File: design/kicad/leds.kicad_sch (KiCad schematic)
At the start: 0 parts

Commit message: completes kicad schematic, starts pcb layout
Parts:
- added C10, C11, C14: 0.1uF, Capacitor_SMD:C_0402_1005Metric, symbol Device:C
- added LED_1, LED_10, LED_11, LED_12, LED_13, LED_14, LED_15, LED_16, LED_17, LED_18, LED_19, LED_2, LED_20, LED_21, LED_22, LED_23, LED_24, LED_25, LED_26, LED_27, LED_28, LED_29, LED_3, LED_30, LED_31, LED_32, LED_33, LED_34, LED_35, LED_36, LED_37, LED_38, LED_39, LED_4, LED_40, LED_41, LED_42, LED_43, LED_44, LED_45, LED_46, LED_47, LED_48, LED_5, LED_6, LED_7, LED_8, LED_9: White, LED_SMD:LED_PLCC-2_3.4x3.0mm_AK, symbol Device:LED
- added R10, R24, R37, R38, R88, R89: 4.7K, Resistor_SMD:R_0603_1608Metric, symbol Device:R
- added R23, R25, R26, R27, R28, R29, R30, R31, R32, R33, R34, R35, R36, R39, R40, R41, R42, R43, R44, R45, R46, R47, R48, R49, R50, R51, R52, R53, R54, R7, R72, R73, R74, R75, R76, R77, R78, R79, R8, R80, R81, R82, R83, R84, R85, R86, R87, R9: 140R, Resistor_SMD:R_0603_1608Metric, symbol Device:R
- added U3, U7, U8: PCA9685PW, Package_SO:TSSOP-28_4.4x9.7mm_P0.65mm, symbol Driver_LED:PCA9685PW
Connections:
- new net: LED_19.1 (K), R41.2
- new net: LED_29.1 (K), R51.2
- new net: LED_36.1 (K), R75.2
- new net: LED_40.1 (K), R79.2
- new net: LED_27.1 (K), R49.2
- new net: LED_23.1 (K), R45.2
- new net: LED_38.1 (K), R77.2
- new net: LED_35.1 (K), R74.2
- new net: LED_14.1 (K), R34.2
- new net: LED_24.1 (K), R46.2
- new net: LED_20.1 (K), R42.2
- new net: LED_39.1 (K), R78.2
- new net: LED_18.1 (K), R40.2
- new net: LED_16.1 (K), R36.2
- new net: LED_45.1 (K), R84.2
- new net: LED_42.1 (K), R81.2
- new net: LED_1.1 (K), R7.2
- new net: LED_25.1 (K), R47.2
- new net: LED_2.1 (K), R8.2
- new net: LED_6.1 (K), R26.2
- new net: LED_17.1 (K), R39.2
- new net: LED_8.1 (K), R28.2
- new net: LED_28.1 (K), R50.2
- new net: LED_34.1 (K), R73.2
- new net: LED_11.1 (K), R31.2
- new net: LED_48.1 (K), R87.2
- new net: LED_26.1 (K), R48.2
- new net: LED_47.1 (K), R86.2
- new net: LED_4.1 (K), R23.2
- new net: LED_5.1 (K), R25.2
- new net: LED_41.1 (K), R80.2
- new net: LED_13.1 (K), R33.2
- new net: LED_31.1 (K), R53.2
- new net: LED_9.1 (K), R29.2
- new net: LED_22.1 (K), R44.2
- new net: LED_32.1 (K), R54.2
- new net: LED_21.1 (K), R43.2
- new net: LED_37.1 (K), R76.2
- new net: LED_43.1 (K), R82.2
- new net: LED_10.1 (K), R30.2
- new net: LED_12.1 (K), R32.2
- new net: LED_30.1 (K), R52.2
- new net: LED_46.1 (K), R85.2
- new net: LED_44.1 (K), R83.2
- new net: LED_3.1 (K), R9.2
- new net: LED_15.1 (K), R35.2
- new net: LED_33.1 (K), R72.2
- new net: LED_7.1 (K), R27.2
- new net 5V: C10.1, C11.1, C14.1, LED_1.2 (A), LED_10.2 (A), LED_11.2 (A), LED_12.2 (A), LED_13.2 (A), LED_14.2 (A), LED_15.2 (A), LED_16.2 (A), LED_17.2 (A), LED_18.2 (A), LED_19.2 (A), LED_2.2 (A), LED_20.2 (A), LED_21.2 (A), LED_22.2 (A), LED_23.2 (A), LED_24.2 (A), LED_25.2 (A), LED_26.2 (A), LED_27.2 (A), LED_28.2 (A), LED_29.2 (A), LED_3.2 (A), LED_30.2 (A), LED_31.2 (A), LED_32.2 (A), LED_33.2 (A), LED_34.2 (A), LED_35.2 (A), LED_36.2 (A), LED_37.2 (A), LED_38.2 (A), LED_39.2 (A), LED_4.2 (A), LED_40.2 (A), LED_41.2 (A), LED_42.2 (A), LED_43.2 (A), LED_44.2 (A), LED_45.2 (A), LED_46.2 (A), LED_47.2 (A), LED_48.2 (A), LED_5.2 (A), LED_6.2 (A), LED_7.2 (A), LED_8.2 (A), LED_9.2 (A), R10.2, R24.2, R37.2, R38.2, R88.2, R89.2, U3.2 (A1), U3.28 (VDD), U7.2 (A1), U7.28 (VDD), U8.2 (A1), U8.28 (VDD)
- new net GND: C10.2, C11.2, C14.2, U3.1 (A0), U3.14 (VSS), U3.23 (~{OE}), U3.24 (A5), U3.25 (EXTCLK), U3.3 (A2), U3.4 (A3), U3.5 (A4), U7.1 (A0), U7.14 (VSS), U7.23 (~{OE}), U7.24 (A5), U7.25 (EXTCLK), U7.3 (A2), U7.4 (A3), U7.5 (A4), U8.1 (A0), U8.14 (VSS), U8.23 (~{OE}), U8.24 (A5), U8.25 (EXTCLK), U8.3 (A2), U8.4 (A3), U8.5 (A4)
- new net LED_1: R7.1, U8.11 (LED5)
- new net LED_10: R30.1, U8.6 (LED0)
- new net LED_11: R31.1, U7.12 (LED6)
- new net LED_12: R32.1, U7.13 (LED7)
- new net LED_13: R33.1, U7.11 (LED5)
- new net LED_14: R34.1, U3.12 (LED6), U7.15 (LED8)
- new net LED_15: R35.1, U3.13 (LED7)
- new net LED_16: R36.1, U3.16 (LED9)
- new net LED_17: R39.1, U3.15 (LED8)
- new net LED_18: R40.1, U3.17 (LED10)
- new net LED_19: R41.1, U3.18 (LED11)
- new net LED_2: R8.1, U8.9 (LED3)
- new net LED_20: R42.1, U8.17 (LED10)
- new net LED_21: R43.1, U8.12 (LED6)
- new net LED_22: R44.1, U8.8 (LED2)
- new net LED_23: R45.1, U7.7 (LED1)
- new net LED_24: R46.1, U7.20 (LED13)
- new net LED_25: R47.1, U7.18 (LED11)
- new net LED_26: R48.1, U3.6 (LED0), U7.16 (LED9)
- new net LED_27: R49.1, U3.8 (LED2)
- new net LED_28: R50.1, U3.10 (LED4)
- new net LED_29: R51.1, U3.19 (LED12)
- new net LED_3: R9.1, U7.8 (LED2)
- new net LED_30: R52.1, U8.10 (LED4)
- new net LED_31: R53.1
- new net LED_32: R54.1, U8.15 (LED8)
- new net LED_33: R72.1, U8.16 (LED9)
- new net LED_34: R73.1, U3.9 (LED3)
- new net LED_35: R74.1, U3.22 (LED15)
- new net LED_36: R75.1, U3.21 (LED14)
- new net LED_37: R76.1, U3.20 (LED13)
- new net LED_38: R77.1, U8.13 (LED7)
- new net LED_39: R78.1, U7.10 (LED4), U7.9 (LED3), U8.7 (LED1)
- new net LED_4: R23.1
- new net LED_40: R79.1, U7.6 (LED0)
- new net LED_41: R80.1, U7.21 (LED14)
- new net LED_42: R81.1, U7.22 (LED15)
- new net LED_43: R82.1
- new net LED_44: R83.1
- new net LED_45: R84.1, U8.19 (LED12)
- new net LED_46: R85.1, U8.20 (LED13)
- new net LED_47: R86.1, U8.21 (LED14)
- new net LED_48: R87.1, U8.22 (LED15)
- new net LED_5: R25.1, U7.19 (LED12)
- new net LED_6: R26.1, U7.17 (LED10)
- new net LED_7: R27.1, U3.7 (LED1)
- new net LED_8: R28.1, U3.11 (LED5)
- new net LED_9: R29.1, U8.18 (LED11)
- new net SCL: R10.1, R37.1, R88.1, U3.26 (SCL), U7.26 (SCL), U8.26 (SCL)
- new net SDA: R24.1, R38.1, R89.1, U3.27 (SDA), U7.27 (SDA), U8.27 (SDA)
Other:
- note added: "Only buttons that can be latched need LEDS, this includes all mod buttons and discludes Empty and Settings. But since there are 16 leds for buttons plus 16 more for modes and side buttons, conservation of leds can be thrown out as a 3rd chip is then required. So no conservation of leds necessary"

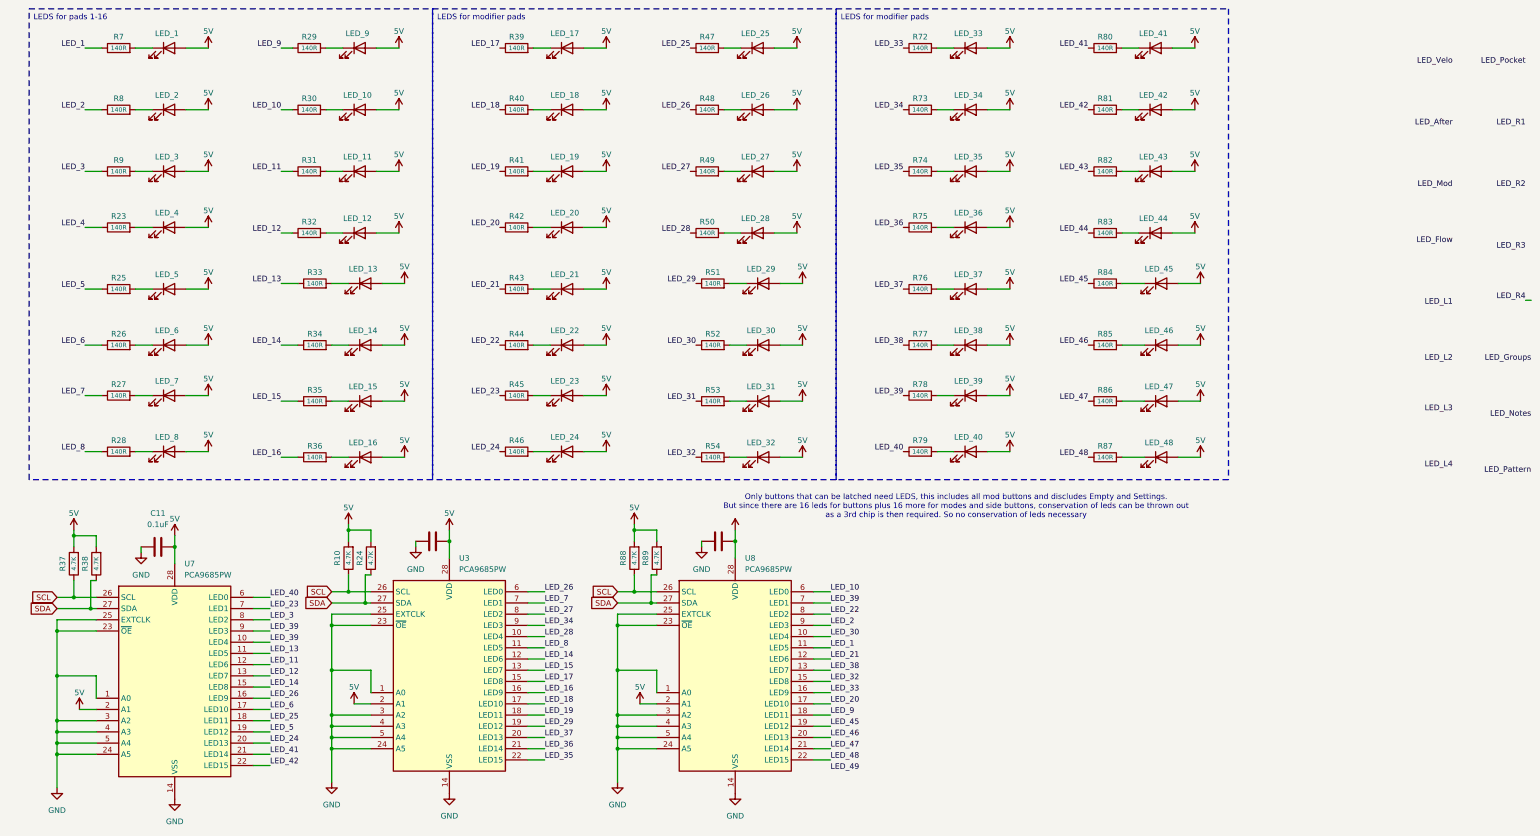
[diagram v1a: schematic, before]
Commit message: routes PCB all except PWR
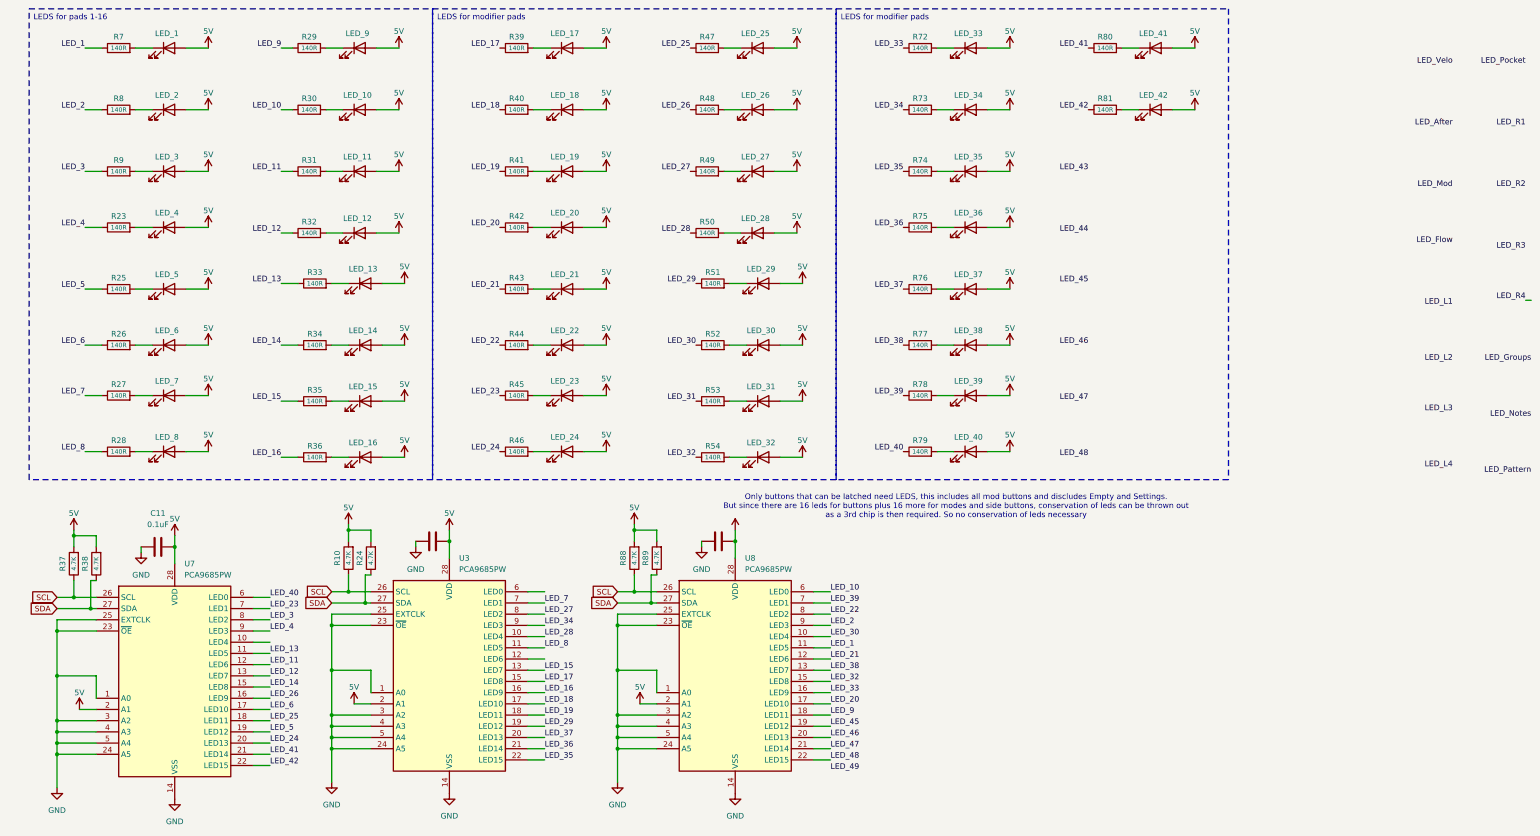
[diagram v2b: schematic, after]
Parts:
- removed LED_43, LED_44, LED_45, LED_46, LED_47, LED_48: White, LED_SMD:LED_PLCC-2_3.4x3.0mm_AK, symbol Device:LED
- removed R82, R83, R84, R85, R86, R87: 140R, Resistor_SMD:R_0603_1608Metric, symbol Device:R
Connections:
- net LED_14: no longer U3.12 (LED6)
- net LED_26: no longer U3.6 (LED0)
- net LED_39: no longer U7.10 (LED4), U7.9 (LED3)
- net LED_4: now also U7.9 (LED3)

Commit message: shortens SD data lines
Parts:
- R23, R25, R26, R27, R28, R29, R30, R31, R32, R33, R34, R35, R36, R39, R40, R41, R42, R43, R44, R45, R46, R47, R48, R49, R50, R51, R52, R53, R54, R7, R72, R73, R74, R75, R76, R77, R78, R79, R8, R80, R81, R9: value 140R -> 150R; LCSC (none) -> C22808
- U3, U7, U8: LCSC C2688894 -> C2678753
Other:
- note added: "was 140R for all LED resistors but not in stock"

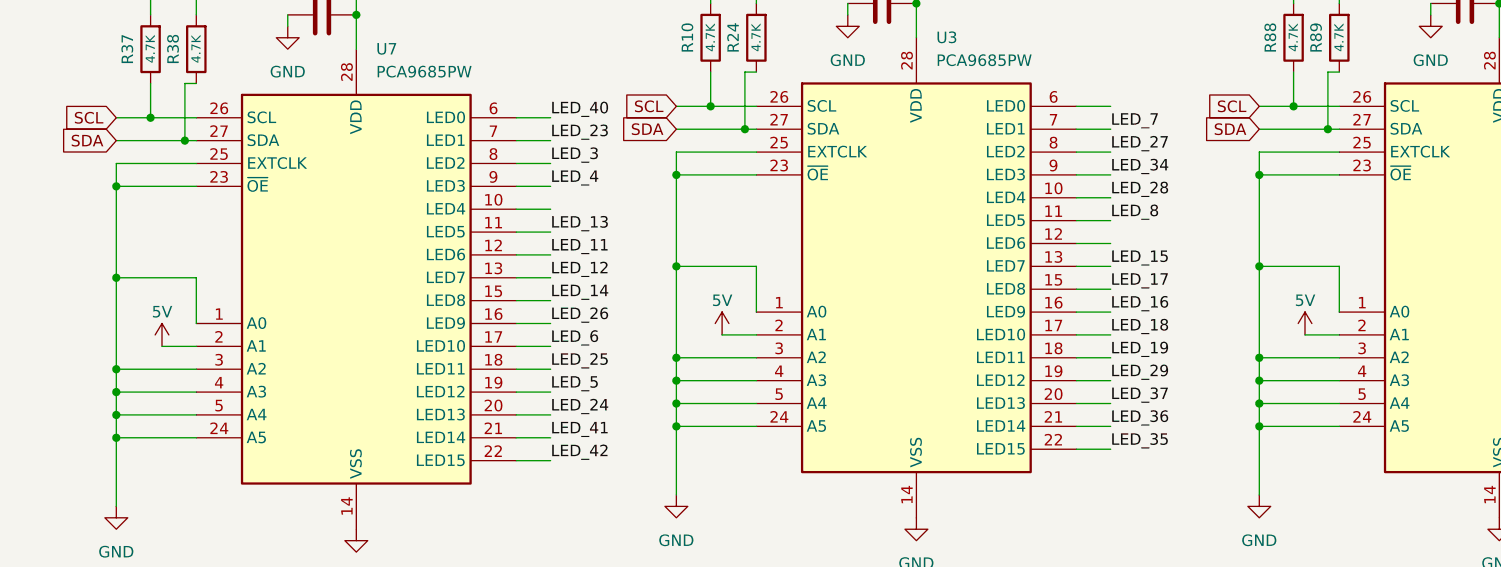
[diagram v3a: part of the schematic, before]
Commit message: pcb rules fixes, reroute suggestions
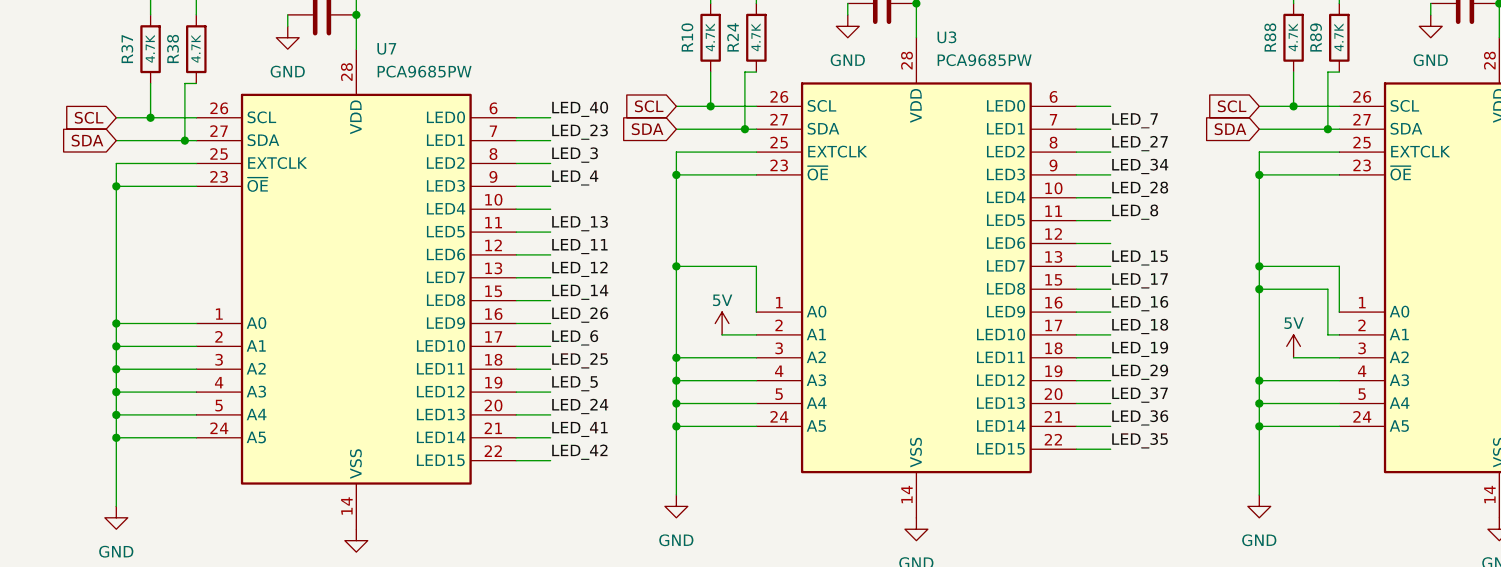
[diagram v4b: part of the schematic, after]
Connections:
- net 5V: now also C14.2, U8.3 (A2); no longer C14.1, U7.2 (A1), U8.2 (A1)
- net GND: now also C14.1, U7.2 (A1), U8.2 (A1); no longer C14.2, U8.3 (A2)
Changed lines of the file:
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@@
 	(paper "A4")
 	(junction
+		(at 146.05 165.1)
+		(diameter 0)
+		(color 0 0 0 0)
+	)
+	(junction
 		(at 146.05 177.8)
 		(diameter 0)
@@
 	)
 	(junction
+		(at 19.05 171.45)
+		(diameter 0)
+		(color 0 0 0 0)
+	)
+	(junction
 		(at 22.86 146.05)
 		(diameter 0)
@@
 	)
 	(junction
-		(at 146.05 175.26)
+		(at 19.05 168.91)
 		(diameter 0)
 		(color 0 0 0 0)
 	)
 	(junction
-		(at 146.05 180.34)
+		(at 146.05 175.26)
 		(diameter 0)
 		(color 0 0 0 0)
 	)
 	(junction
-		(at 19.05 176.53)
+		(at 146.05 180.34)
 		(diameter 0)
 		(color 0 0 0 0)
 	)
 	(junction
-		(at 149.86 130.81)
+		(at 19.05 176.53)
 		(diameter 0)
 		(color 0 0 0 0)
 	)
 	(junction
-		(at 19.05 163.83)
+		(at 149.86 130.81)
 		(diameter 0)
 		(color 0 0 0 0)
@@
 	)
 	(junction
-		(at 146.05 172.72)
-		(diameter 0)
-		(color 0 0 0 0)
-	)
-	(junction
 		(at 85.09 144.78)
 		(diameter 0)
@@
 	(wire
 		(pts
-			(xy 27.94 168.91) (xy 27.94 163.83)
-		)
-		(stroke
-			(width 0)
-			(type default)
-		)
-	)
-	(wire
-		(pts
 			(xy 97.79 74.93) (xy 92.71 74.93)
 		)
@@
 	(wire
 		(pts
+			(xy 154.94 170.18) (xy 153.67 170.18)
+		)
+		(stroke
+			(width 0)
+			(type default)
+		)
+	)
+	(wire
+		(pts
 			(xy 143.51 100.33) (xy 138.43 100.33)
 		)
@@
 	(wire
 		(pts
-			(xy 151.13 170.18) (xy 154.94 170.18)
+			(xy 153.67 165.1) (xy 146.05 165.1)
 		)
 		(stroke
@@
 	(wire
 		(pts
+			(xy 149.86 172.72) (xy 154.94 172.72)
+		)
+		(stroke
+			(width 0)
+			(type default)
+		)
+	)
+	(wire
+		(pts
 			(xy 67.31 153.67) (xy 63.5 153.67)
 		)
@@
 	(wire
 		(pts
-			(xy 154.94 172.72) (xy 146.05 172.72)
-		)
-		(stroke
-			(width 0)
-			(type default)
-		)
-	)
-	(wire
-		(pts
 			(xy 53.34 76.2) (xy 48.26 76.2)
 		)
@@
 	(wire
 		(pts
-			(xy 19.05 153.67) (xy 19.05 163.83)
+			(xy 153.67 170.18) (xy 153.67 165.1)
 		)
 		(stroke
@@
 	(wire
 		(pts
-			(xy 24.13 171.45) (xy 27.94 171.45)
-		)
-		(stroke
-			(width 0)
-			(type default)
-		)
-	)
-	(wire
-		(pts
 			(xy 81.28 162.56) (xy 81.28 172.72)
 		)
@@
 	(wire
 		(pts
+			(xy 19.05 168.91) (xy 19.05 171.45)
+		)
+		(stroke
+			(width 0)
+			(type default)
+		)
+	)
+	(wire
+		(pts
 			(xy 67.31 176.53) (xy 63.5 176.53)
 		)
@@
 	(wire
 		(pts
-			(xy 146.05 172.72) (xy 146.05 175.26)
+			(xy 146.05 162.56) (xy 146.05 165.1)
 		)
 		(stroke
@@
 	(wire
 		(pts
-			(xy 19.05 163.83) (xy 19.05 173.99)
+			(xy 19.05 153.67) (xy 19.05 168.91)
 		)
 		(stroke
@@
 	(wire
 		(pts
+			(xy 146.05 165.1) (xy 146.05 175.26)
+		)
+		(stroke
+			(width 0)
+			(type default)
+		)
+	)
+	(wire
+		(pts
 			(xy 194.31 182.88) (xy 190.5 182.88)
 		)
@@
 	(wire
 		(pts
+			(xy 19.05 171.45) (xy 27.94 171.45)
+		)
+		(stroke
+			(width 0)
+			(type default)
+		)
+	)
+	(wire
+		(pts
 			(xy 154.94 140.97) (xy 153.67 140.97)
 		)
@@
 	(wire
 		(pts
-			(xy 27.94 163.83) (xy 19.05 163.83)
+			(xy 27.94 168.91) (xy 19.05 168.91)
 		)
 		(stroke
@@
 	(wire
 		(pts
-			(xy 146.05 162.56) (xy 146.05 172.72)
+			(xy 67.31 166.37) (xy 63.5 166.37)
 		)
 		(stroke
@@
 	(wire
 		(pts
-			(xy 67.31 166.37) (xy 63.5 166.37)
+			(xy 234.95 21.59) (xy 229.87 21.59)
 		)
 		(stroke
@@
 	(wire
 		(pts
-			(xy 234.95 21.59) (xy 229.87 21.59)
+			(xy 351.79 78.74) (xy 353.06 78.74)
 		)
 		(stroke
@@
 	(wire
 		(pts
-			(xy 351.79 78.74) (xy 353.06 78.74)
+			(xy 67.31 146.05) (xy 63.5 146.05)
 		)
 		(stroke
@@
 	(wire
 		(pts
-			(xy 67.31 146.05) (xy 63.5 146.05)
+			(xy 19.05 171.45) (xy 19.05 173.99)
 		)
 		(stroke
@@
 	)
 	(symbol
-		(lib_id "daisy_seed:3V3_D")
-		(at 24.13 171.45 0)
-		(unit 1)
-		(exclude_from_sim no)
-		(in_bom yes)
-		(on_board yes)
-		(dnp no)
-		(fields_autoplaced yes)
-		(property "Reference" "#PWR055"
-			(at 27.94 172.72 0)
-			(effects
-				(font
-					(size 1.27 1.27)
-				)
-				(hide yes)
-			)
-		)
-		(property "Value" "5V"
-			(at 24.13 167.64 0)
-			(effects
-				(font
-					(size 1.27 1.27)
-				)
-			)
-		)
-		(property "Footprint" ""
-			(at 24.13 171.45 0)
-			(effects
-				(font
-					(size 1.27 1.27)
-				)
-				(hide yes)
-			)
-		)
-		(property "Datasheet" ""
-			(at 24.13 171.45 0)
-			(effects
-				(font
-					(size 1.27 1.27)
-				)
-				(hide yes)
-			)
-		)
-		(property "Description" ""
-			(at 24.13 171.45 0)
-			(effects
-				(font
-					(size 1.27 1.27)
-				)
-				(hide yes)
-			)
-		)
-		(pin "1"
-		)
-		(instances
-			(project "soundpad"
-				(path "/e7f7d9eb-c978-4dc1-9b91-2f2a4525cbe7/9194bf31-8079-4b2f-befe-901822c457d4"
-					(reference "#PWR055")
-					(unit 1)
-				)
-			)
-		)
-	)
-	(symbol
 		(lib_id "Device:LED")
 		(at 177.8 21.59 0)
@@
 	(symbol
 		(lib_id "daisy_seed:3V3_D")
-		(at 151.13 170.18 0)
+		(at 149.86 172.72 0)
 		(unit 1)
 		(exclude_from_sim no)
@@
 		(fields_autoplaced yes)
 		(property "Reference" "#PWR0118"
-			(at 154.94 171.45 0)
+			(at 153.67 173.99 0)
 			(effects
 				(font
@@
 		)
 		(property "Value" "5V"
-			(at 151.13 166.37 0)
+			(at 149.86 168.91 0)
 			(effects
 				(font
@@
 		)
 		(property "Footprint" ""
-			(at 151.13 170.18 0)
+			(at 149.86 172.72 0)
 			(effects
 				(font
@@
 		)
 		(property "Datasheet" ""
-			(at 151.13 170.18 0)
+			(at 149.86 172.72 0)
 			(effects
 				(font
@@
 		)
 		(property "Description" ""
-			(at 151.13 170.18 0)
+			(at 149.86 172.72 0)
 			(effects
 				(font
@@
 	(symbol
 		(lib_id "Device:C")
-		(at 168.91 133.35 270)
+		(at 168.91 133.35 90)
+		(mirror x)
 		(unit 1)
 		(exclude_from_sim no)
@@
 		(on_board yes)
 		(dnp no)
-		(fields_autoplaced yes)
 		(property "Reference" "C14"
 			(at 168.91 125.73 90)
@@
 		)
 		(property "Footprint" "Capacitor_SMD:C_0402_1005Metric"
-			(at 165.1 134.3152 0)
+			(at 172.72 134.3152 0)
 			(effects
 				(font
